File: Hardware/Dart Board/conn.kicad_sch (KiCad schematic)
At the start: 2 parts, among them J1 Conn_01x20_Socket, J2 Conn_01x20_Socket

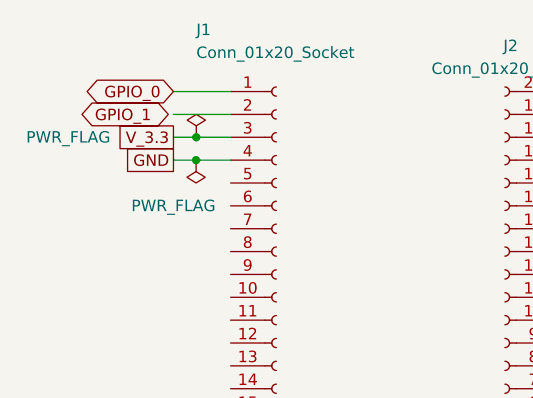
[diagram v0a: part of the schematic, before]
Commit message: Update conn.kicad_sch
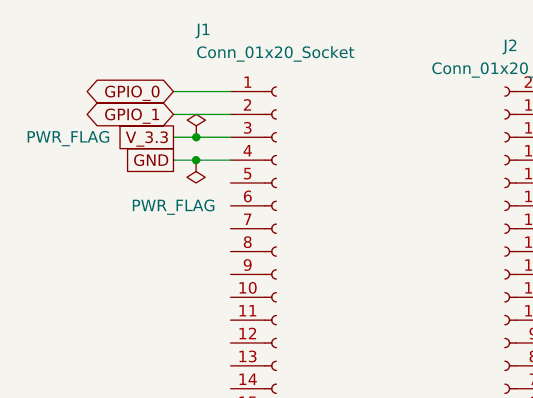
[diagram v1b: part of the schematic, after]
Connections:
- net GPIO_1: now also J1.2 (Pin_2)
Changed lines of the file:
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@@
 	(global_label "GPIO_1"
 		(shape bidirectional)
-		(at 20.32 38.1 0)
+		(at 30.48 38.1 180)
 		(fields_autoplaced yes)
 		(effects
@@
 				(size 1.27 1.27)
 			)
-			(justify left)
+			(justify right)
 		)
 		(property "Intersheetrefs" "${INTERSHEET_REFS}"
-			(at 31.0689 38.1 0)
+			(at 19.7311 38.1 0)
 			(effects
 				(font
 					(size 1.27 1.27)
 				)
-				(justify left)
+				(justify right)
 				(hide yes)
 			)

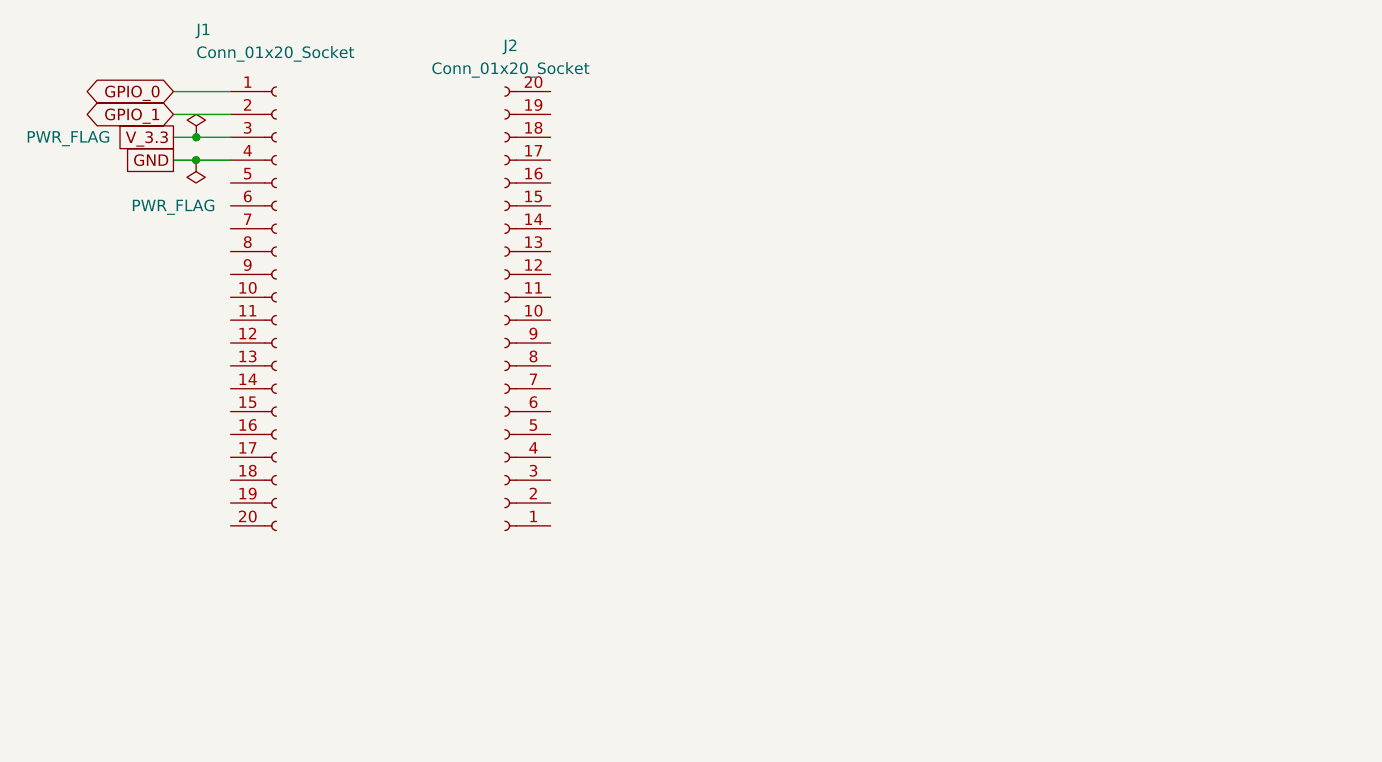
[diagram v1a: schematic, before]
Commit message: Added OPS2 Dev Board to library and schematic
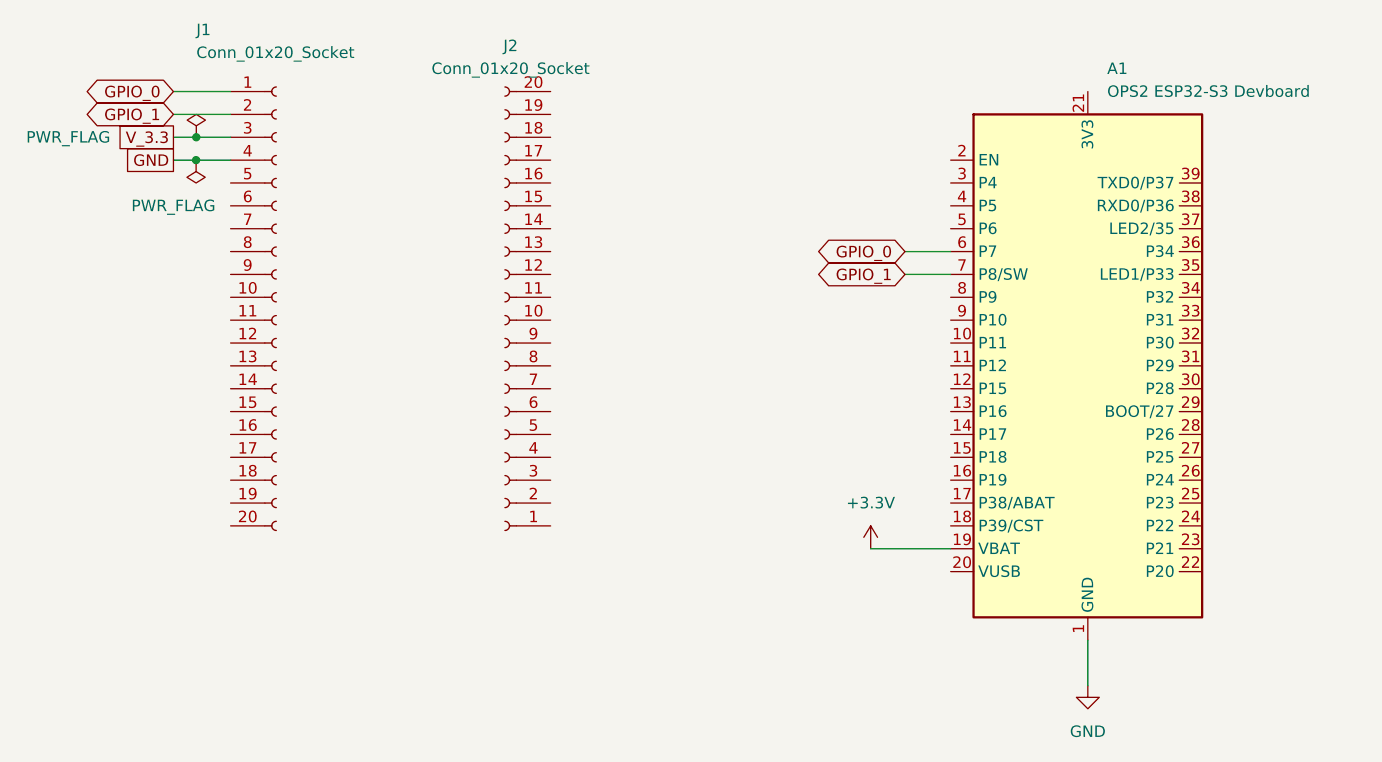
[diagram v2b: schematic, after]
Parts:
- added A1: OPS2 ESP32-S3 Devboard, IEEE_OPS2:ESP32_Devboard, symbol IEEE_OPS2:ESP32_Devboard
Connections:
- net GND: now also A1.1 (GND), A1.40 (GND)
- net GPIO_0: now also A1.6 (P7)
- net GPIO_1: now also A1.7 (P8/SW)
- new net +3.3V: A1.19 (VBAT)
